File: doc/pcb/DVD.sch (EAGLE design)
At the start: 32 parts, among them IC1 7805, IC2 74HC14N

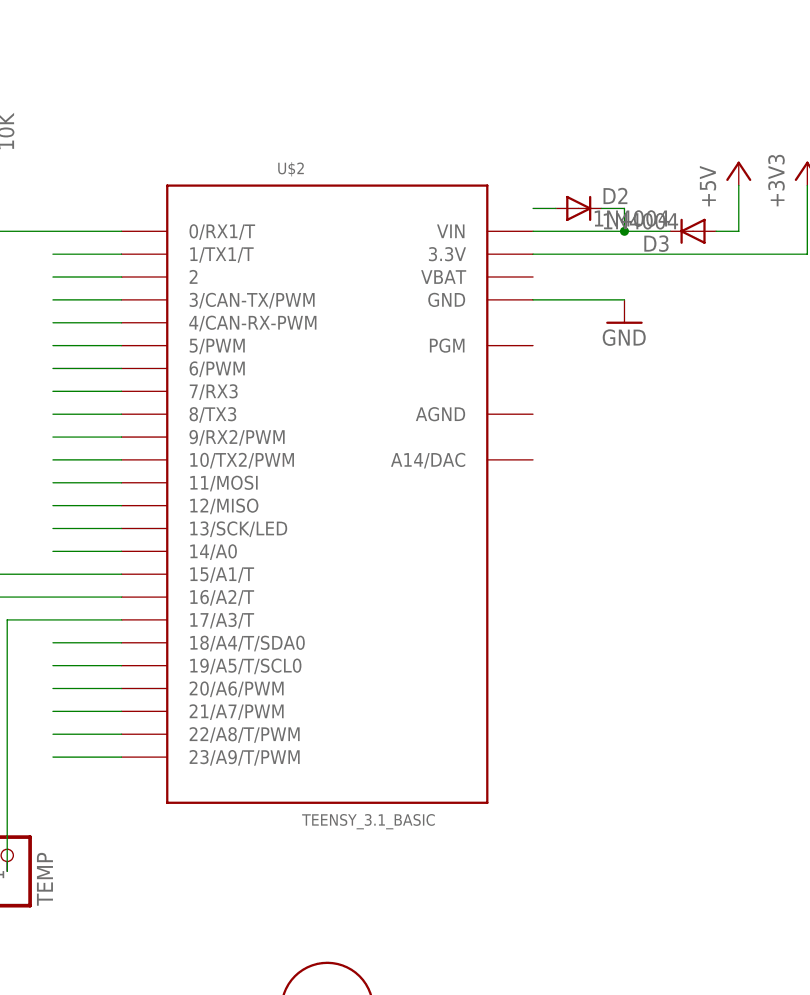
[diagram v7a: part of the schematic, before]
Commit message: PCB removed not connected pins from Teensy
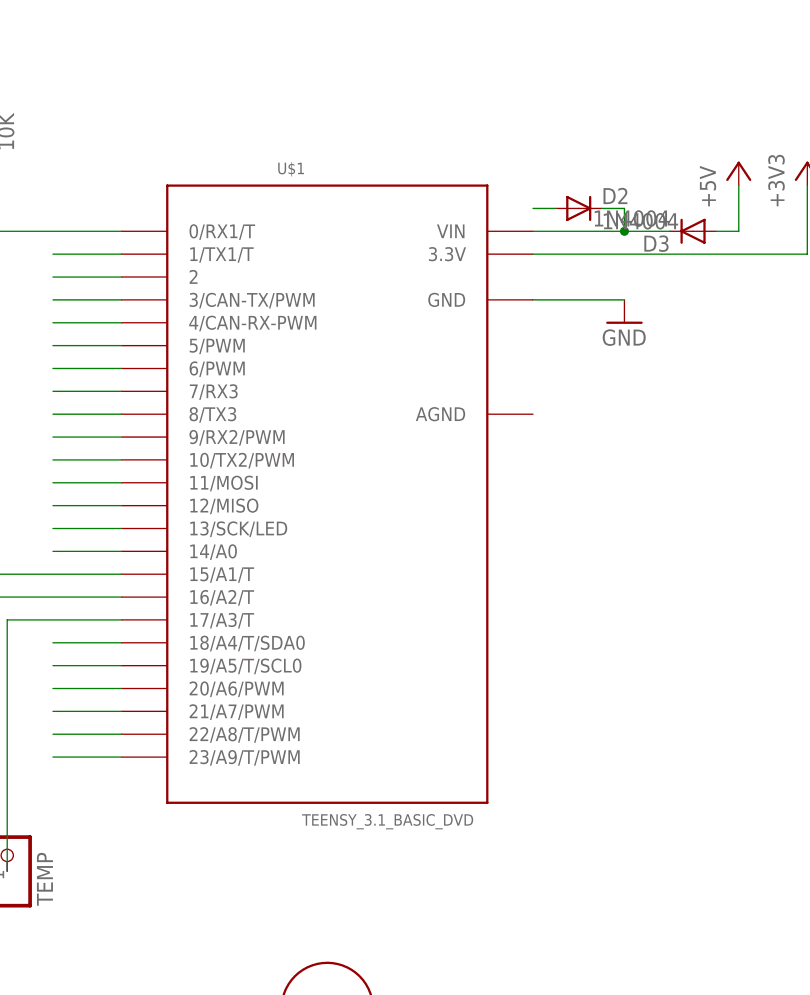
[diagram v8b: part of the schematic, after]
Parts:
- removed U$2: TEENSY_3.1_BASIC, Teensy_3_Series_Board_v1.0:TEENSY_3.1_BASIC
- added U$1: TEENSY_3.1_BASIC_DVD, Teensy_3_Series_Board_v1.0:TEENSY_3.1_BASIC_DVD
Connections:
- net +3V3: now also U$1.3.3V; no longer U$2.3.3V
- net CE: now also U$1.8/TX3; no longer U$2.8/TX3
- net CSN_RADIO: now also U$1.10/TX2/PWM; no longer U$2.10/TX2/PWM
- net CSN_SD: now also U$1.9/RX2/PWM; no longer U$2.9/RX2/PWM
- net D4_IR: now also U$1.4/CAN-RX-PWM; no longer U$2.4/CAN-RX-PWM
- net GND: now also U$1.GND; no longer U$2.GND
- net IN1: now also U$1.23/A9/T/PWM; no longer U$2.23/A9/T/PWM
- net IN2: now also U$1.22/A8/T/PWM; no longer U$2.22/A8/T/PWM
- net JP0: now also U$1.17/A3/T; no longer U$2.17/A3/T
- net MISO: now also U$1.12/MISO; no longer U$2.12/MISO
- net MOSI: now also U$1.11/MOSI; no longer U$2.11/MOSI
- net N$1: now also U$1.VIN; no longer U$2.VIN
- net N$10: now also U$1.15/A1/T; no longer U$2.15/A1/T
- net N$11: now also U$1.16/A2/T; no longer U$2.16/A2/T
- net N$18: now also U$1.0/RX1/T; no longer U$2.0/RX1/T
- net N$19: now also U$1.1/TX1/T; no longer U$2.1/TX1/T
- net N$20: now also U$1.2; no longer U$2.2
- net N$21: now also U$1.6/PWM; no longer U$2.6/PWM
- net N$22: now also U$1.7/RX3; no longer U$2.7/RX3
- net N$3: now also U$1.5/PWM; no longer U$2.5/PWM
- net N$9: now also U$1.13/SCK/LED; no longer U$2.13/SCK/LED
- net PWM: now also U$1.21/A7/PWM; no longer U$2.21/A7/PWM
- net SCK: now also U$1.14/A0; no longer U$2.14/A0
- net SCL: now also U$1.19/A5/T/SCL0; no longer U$2.19/A5/T/SCL0
- net SDA: now also U$1.18/A4/T/SDA0; no longer U$2.18/A4/T/SDA0
- net SPEED_SENSOR: now also U$1.3/CAN-TX/PWM; no longer U$2.3/CAN-TX/PWM
- net STBY: now also U$1.20/A6/PWM; no longer U$2.20/A6/PWM
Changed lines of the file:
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@@
 <part name="D2" library="adafruit" deviceset="1N4004" device=""/>
 <part name="D3" library="adafruit" deviceset="1N4004" device=""/>
-<part name="U$2" library="Teensy_3_Series_Board_v1.0" deviceset="TEENSY_3.1_BASIC" device=""/>
 <part name="POLULU_TB6612FNG" library="ic-package_mod" deviceset="DIL16W" device="" value="DIL16W"/>
 <part name="BNO055" library="ic-package_mod" deviceset="DIL10-6-4" device=""/>
+<part name="U$1" library="Teensy_3_Series_Board_v1.0" deviceset="TEENSY_3.1_BASIC_DVD" device=""/>
 </parts>
 <sheets>
@@
 <instance part="D2" gate="1" x="144.78" y="142.24"/>
 <instance part="D3" gate="1" x="157.48" y="139.7" rot="R180"/>
-<instance part="U$2" gate="G$1" x="116.84" y="111.76"/>
 <instance part="POLULU_TB6612FNG" gate="G$1" x="20.32" y="33.02"/>
 <instance part="BNO055" gate="G$1" x="187.96" y="137.16" rot="MR0"/>
+<instance part="U$1" gate="G$1" x="116.84" y="111.76"/>
 </instances>
 <busses>
@@
 <pinref part="GND2" gate="1" pin="GND"/>
 <wire x1="139.7" y1="132.08" x2="149.86" y2="132.08" width="0.1524" layer="91"/>
-<pinref part="U$2" gate="G$1" pin="GND"/>
+<pinref part="U$1" gate="G$1" pin="GND"/>
 </segment>
 <segment>
@@
 <segment>
 <wire x1="93.98" y1="129.54" x2="86.36" y2="129.54" width="0.1524" layer="91"/>
-<pinref part="U$2" gate="G$1" pin="4/CAN-RX-PWM"/>
+<pinref part="U$1" gate="G$1" pin="4/CAN-RX-PWM"/>
 </segment>
 </net>
@@
 <segment>
 <wire x1="93.98" y1="127" x2="86.36" y2="127" width="0.1524" layer="91"/>
-<pinref part="U$2" gate="G$1" pin="5/PWM"/>
+<pinref part="U$1" gate="G$1" pin="5/PWM"/>
 </segment>
 </net>
@@
 <segment>
 <wire x1="93.98" y1="106.68" x2="86.36" y2="106.68" width="0.1524" layer="91"/>
-<pinref part="U$2" gate="G$1" pin="13/SCK/LED"/>
+<pinref part="U$1" gate="G$1" pin="13/SCK/LED"/>
 </segment>
 </net>
@@
 <wire x1="60.96" y1="101.6" x2="93.98" y2="101.6" width="0.1524" layer="91"/>
 <junction x="60.96" y="101.6"/>
-<pinref part="U$2" gate="G$1" pin="15/A1/T"/>
+<pinref part="U$1" gate="G$1" pin="15/A1/T"/>
 </segment>
 </net>
@@
 <wire x1="93.98" y1="99.06" x2="68.58" y2="99.06" width="0.1524" layer="91"/>
 <junction x="68.58" y="99.06"/>
-<pinref part="U$2" gate="G$1" pin="16/A2/T"/>
+<pinref part="U$1" gate="G$1" pin="16/A2/T"/>
 </segment>
 </net>
@@
 <junction x="78.74" y="144.78"/>
 <pinref part="JP4" gate="G$1" pin="1"/>
-<pinref part="U$2" gate="G$1" pin="0/RX1/T"/>
+<pinref part="U$1" gate="G$1" pin="0/RX1/T"/>
 </segment>
 </net>
@@
 <segment>
 <wire x1="93.98" y1="137.16" x2="86.36" y2="137.16" width="0.1524" layer="91"/>
-<pinref part="U$2" gate="G$1" pin="1/TX1/T"/>
+<pinref part="U$1" gate="G$1" pin="1/TX1/T"/>
 </segment>
 </net>
@@
 <segment>
 <wire x1="93.98" y1="134.62" x2="86.36" y2="134.62" width="0.1524" layer="91"/>
-<pinref part="U$2" gate="G$1" pin="2"/>
+<pinref part="U$1" gate="G$1" pin="2"/>
 </segment>
 </net>
@@
 <segment>
 <wire x1="93.98" y1="124.46" x2="86.36" y2="124.46" width="0.1524" layer="91"/>
-<pinref part="U$2" gate="G$1" pin="6/PWM"/>
+<pinref part="U$1" gate="G$1" pin="6/PWM"/>
 </segment>
 </net>
@@
 <segment>
 <wire x1="93.98" y1="121.92" x2="86.36" y2="121.92" width="0.1524" layer="91"/>
-<pinref part="U$2" gate="G$1" pin="7/RX3"/>
+<pinref part="U$1" gate="G$1" pin="7/RX3"/>
 </segment>
 </net>
@@
 <pinref part="JP10" gate="G$1" pin="1"/>
 <wire x1="81.28" y1="68.58" x2="81.28" y2="96.52" width="0.1524" layer="91"/>
-<pinref part="U$2" gate="G$1" pin="17/A3/T"/>
+<pinref part="U$1" gate="G$1" pin="17/A3/T"/>
 </segment>
 </net>
@@
 <segment>
 <wire x1="93.98" y1="88.9" x2="86.36" y2="88.9" width="0.1524" layer="91"/>
-<pinref part="U$2" gate="G$1" pin="20/A6/PWM"/>
+<pinref part="U$1" gate="G$1" pin="20/A6/PWM"/>
 </segment>
 <segment>
@@
 <pinref part="+3V1" gate="G$1" pin="+3V3"/>
 <wire x1="170.18" y1="137.16" x2="170.18" y2="144.78" width="0.1524" layer="91"/>
-<pinref part="U$2" gate="G$1" pin="3.3V"/>
+<pinref part="U$1" gate="G$1" pin="3.3V"/>
 </segment>
 <segment>
@@
 <segment>
 <wire x1="93.98" y1="132.08" x2="86.36" y2="132.08" width="0.1524" layer="91"/>
-<pinref part="U$2" gate="G$1" pin="3/CAN-TX/PWM"/>
+<pinref part="U$1" gate="G$1" pin="3/CAN-TX/PWM"/>
 </segment>
 </net>
@@
 <segment>
 <wire x1="93.98" y1="116.84" x2="86.36" y2="116.84" width="0.1524" layer="91"/>
-<pinref part="U$2" gate="G$1" pin="9/RX2/PWM"/>
+<pinref part="U$1" gate="G$1" pin="9/RX2/PWM"/>
 </segment>
 </net>
@@
 <segment>
 <wire x1="93.98" y1="104.14" x2="86.36" y2="104.14" width="0.1524" layer="91"/>
-<pinref part="U$2" gate="G$1" pin="14/A0"/>
+<pinref part="U$1" gate="G$1" pin="14/A0"/>
 </segment>
 <segment>
@@
 <segment>
 <wire x1="93.98" y1="111.76" x2="86.36" y2="111.76" width="0.1524" layer="91"/>
-<pinref part="U$2" gate="G$1" pin="11/MOSI"/>
+<pinref part="U$1" gate="G$1" pin="11/MOSI"/>
 </segment>
 <segment>
@@
 <segment>
 <wire x1="93.98" y1="109.22" x2="86.36" y2="109.22" width="0.1524" layer="91"/>
-<pinref part="U$2" gate="G$1" pin="12/MISO"/>
+<pinref part="U$1" gate="G$1" pin="12/MISO"/>
 </segment>
 <segment>
@@
 <segment>
 <wire x1="93.98" y1="114.3" x2="86.36" y2="114.3" width="0.1524" layer="91"/>
-<pinref part="U$2" gate="G$1" pin="10/TX2/PWM"/>
+<pinref part="U$1" gate="G$1" pin="10/TX2/PWM"/>
 </segment>
 </net>
@@
 <segment>
 <wire x1="93.98" y1="119.38" x2="86.36" y2="119.38" width="0.1524" layer="91"/>
-<pinref part="U$2" gate="G$1" pin="8/TX3"/>
+<pinref part="U$1" gate="G$1" pin="8/TX3"/>
 </segment>
 </net>
@@
 <segment>
 <wire x1="93.98" y1="93.98" x2="86.36" y2="93.98" width="0.1524" layer="91"/>
-<pinref part="U$2" gate="G$1" pin="18/A4/T/SDA0"/>
+<pinref part="U$1" gate="G$1" pin="18/A4/T/SDA0"/>
 </segment>
 </net>
@@
 <segment>
 <wire x1="93.98" y1="91.44" x2="86.36" y2="91.44" width="0.1524" layer="91"/>
-<pinref part="U$2" gate="G$1" pin="19/A5/T/SCL0"/>
+<pinref part="U$1" gate="G$1" pin="19/A5/T/SCL0"/>
 </segment>
 </net>
@@
 <segment>
 <wire x1="93.98" y1="81.28" x2="86.36" y2="81.28" width="0.1524" layer="91"/>
-<pinref part="U$2" gate="G$1" pin="23/A9/T/PWM"/>
+<pinref part="U$1" gate="G$1" pin="23/A9/T/PWM"/>
 </segment>
 </net>
@@
 <segment>
 <wire x1="93.98" y1="83.82" x2="86.36" y2="83.82" width="0.1524" layer="91"/>
-<pinref part="U$2" gate="G$1" pin="22/A8/T/PWM"/>
+<pinref part="U$1" gate="G$1" pin="22/A8/T/PWM"/>
 </segment>
 </net>
@@
 <segment>
 <wire x1="93.98" y1="86.36" x2="86.36" y2="86.36" width="0.1524" layer="91"/>
-<pinref part="U$2" gate="G$1" pin="21/A7/PWM"/>
+<pinref part="U$1" gate="G$1" pin="21/A7/PWM"/>
 </segment>
 </net>
@@
 <wire x1="149.86" y1="142.24" x2="149.86" y2="139.7" width="0.1524" layer="91"/>
 <junction x="149.86" y="139.7"/>
-<pinref part="U$2" gate="G$1" pin="VIN"/>
-</segment>
-</net>
+<pinref part="U$1" gate="G$1" pin="VIN"/>
+</segment>
+</net>
